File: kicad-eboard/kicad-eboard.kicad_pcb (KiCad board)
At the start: 2 copper layers, 94 parts, among them J1 Conn_02x03, J2 Conn_01x02, J3 Conn_01x10, M1 Hopper_Servo, SW1 LIMIT_1, SW2 LIMIT_2, SW3 SRX_Encoder, U1 TinkerBoard, U10 REF2033, U11 PDQ15-Q24-S12-D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

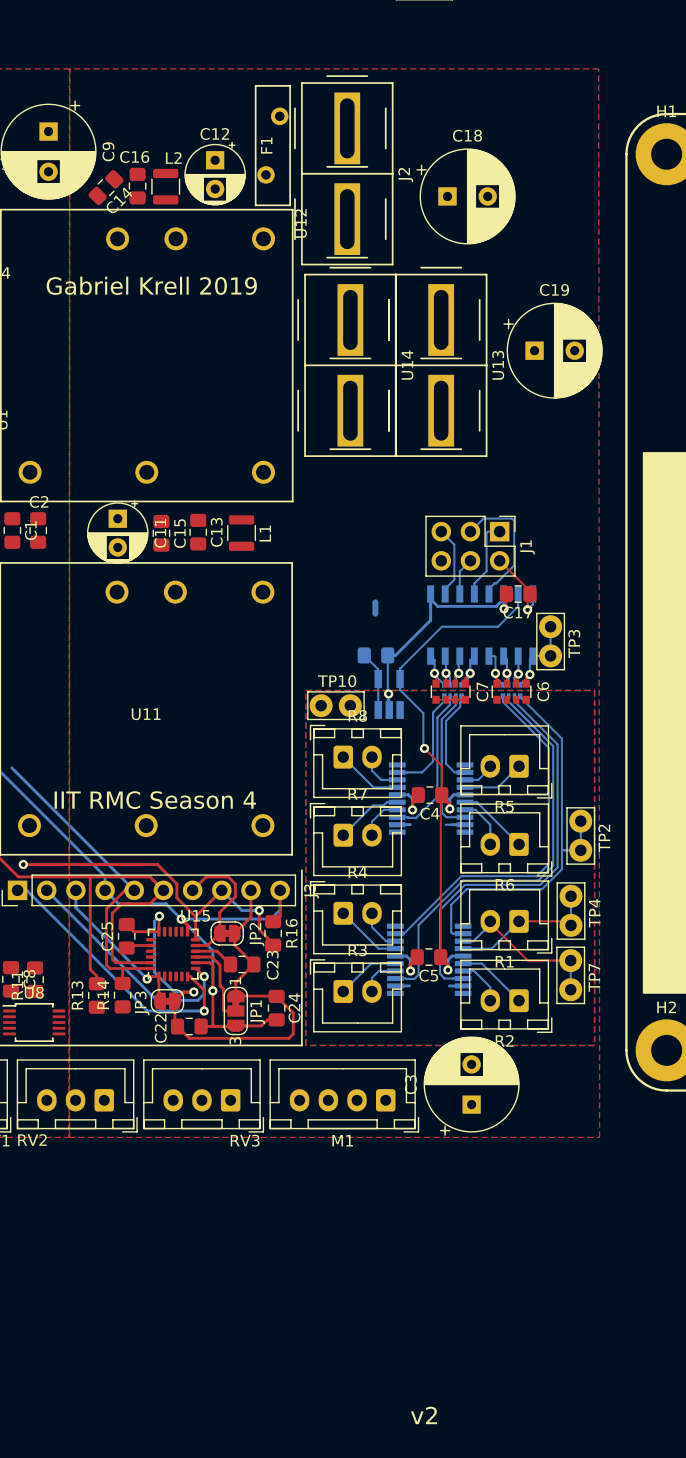
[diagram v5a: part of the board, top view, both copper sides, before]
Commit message: Swap M1,m2 current sense
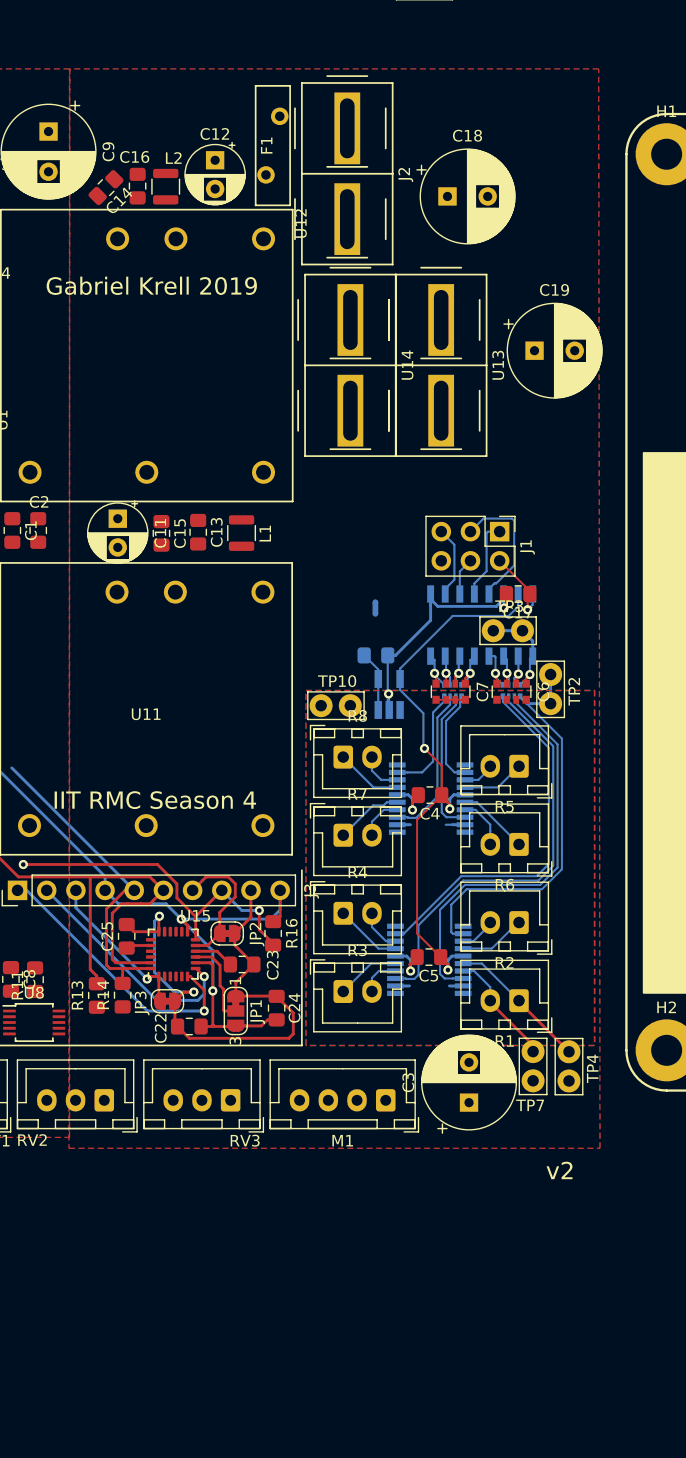
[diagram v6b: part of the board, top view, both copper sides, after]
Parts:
- moved TP4 13.5 mm to (91.3, 100.4)
- moved TP2 13.0 mm to (89.7, 67.5)
- moved TP7 8.58 mm to (88.2, 100.4)
- moved R1 6.90 mm to (87.0, 93.4)
- moved R2 6.80 mm to (87.0, 86.6)
- moved TP3 3.29 mm to (87.2, 61.2), turned to 180 degrees
- moved C3 0.29 mm to (82.6, 102.3)
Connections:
- U6 pad 3: /M1- -> /M2-
- U6 pad 4: /M1+ -> /M2+
- U6 pad 6: /M2+ -> /M1+
- U6 pad 7: /M2- -> /M1-
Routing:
- net /M1-: track 14.3 -> 10.1 mm
- net +3.3VADC: track 47.8 -> 49.5 mm
- net Net-(R9-Pad1): track 35.1 -> 36.4 mm
- net /M1+: track 13.5 -> 12.5 mm
- net Net-(C6-Pad1): track 7.98 -> 9.00 mm
- net /M2-: track 4.12 -> 3.23 mm

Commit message: Routing taking shape
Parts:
- removed C19: 470u, Capacitor_THT:CP_Radial_D8.0mm_P3.50mm
- C10: moved to F.Cu
- moved TP10 16.1 mm to (88.4, 67.6), turned to 90 degrees
- moved C6 14.9 mm to (71.4, 66.2)
- moved R9 14.9 mm to (71.4, 66.1)
- moved J1 9.70 mm to (75.6, 52.3)
- moved TP3 9.70 mm to (77.5, 61.0)
- moved U9 9.70 mm to (74.0, 60.5)
- moved C17 9.70 mm to (77.2, 57.8)
- moved TP2 9.61 mm to (80.2, 66.3)
- moved U10 9.43 mm to (85.1, 66.3)
- moved C10 8.52 mm to (82.6, 65.9), turned to 270 degrees
- moved NT1 7.15 mm to (67.8, 56.7)
- moved C7 4.48 mm to (76.5, 66.3)
- moved R10 4.48 mm to (76.7, 66.2)
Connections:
- TP2 pad 1: Net-(R9-Pad1) -> Net-(R10-Pad1)
- TP3 pad 1: Net-(C6-Pad1) -> Net-(C7-Pad1)
- U9 pad 1: Net-(C6-Pad1) -> Net-(C7-Pad1)
- U9 pad 2: Net-(C6-Pad2) -> Net-(C7-Pad2)
- U9 pad 3: Net-(C6-Pad3) -> Net-(C7-Pad3)
- U9 pad 4: Net-(C6-Pad4) -> Net-(C7-Pad4)
- U9 pad 5: Net-(C7-Pad1) -> Net-(C6-Pad1)
- U9 pad 6: Net-(C7-Pad2) -> Net-(C6-Pad2)
- U9 pad 7: Net-(C7-Pad3) -> Net-(C6-Pad3)
- U9 pad 8: Net-(C7-Pad4) -> Net-(C6-Pad4)
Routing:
- net GNDREF: track 34.2 -> 25.3 mm
- net Net-(R10-Pad1): track 8.40 -> 14.7 mm
- net Net-(R9-Pad1): track 36.4 -> 30.8 mm
- net Net-(C6-Pad1): track 9.00 -> 3.84 mm
- net Net-(C7-Pad1): track 4.04 -> 9.12 mm
- net +5V: track 5.26 -> 9.19 mm, vias 0 -> 1
- net /M1-: track 10.1 -> 12.6 mm
- net /M1+: track 12.5 -> 15.0 mm
- net Net-(R9-Pad4): track 32.1 -> 30.0 mm
- net Net-(R9-Pad3): track 36.7 -> 34.7 mm
- net Net-(R10-Pad4): track 9.59 -> 8.37 mm
- net Net-(R10-Pad2): track 12.9 -> 14.0 mm
- net +3.3VADC: track 49.5 -> 48.7 mm
- net Net-(R9-Pad2): track 36.0 -> 35.2 mm

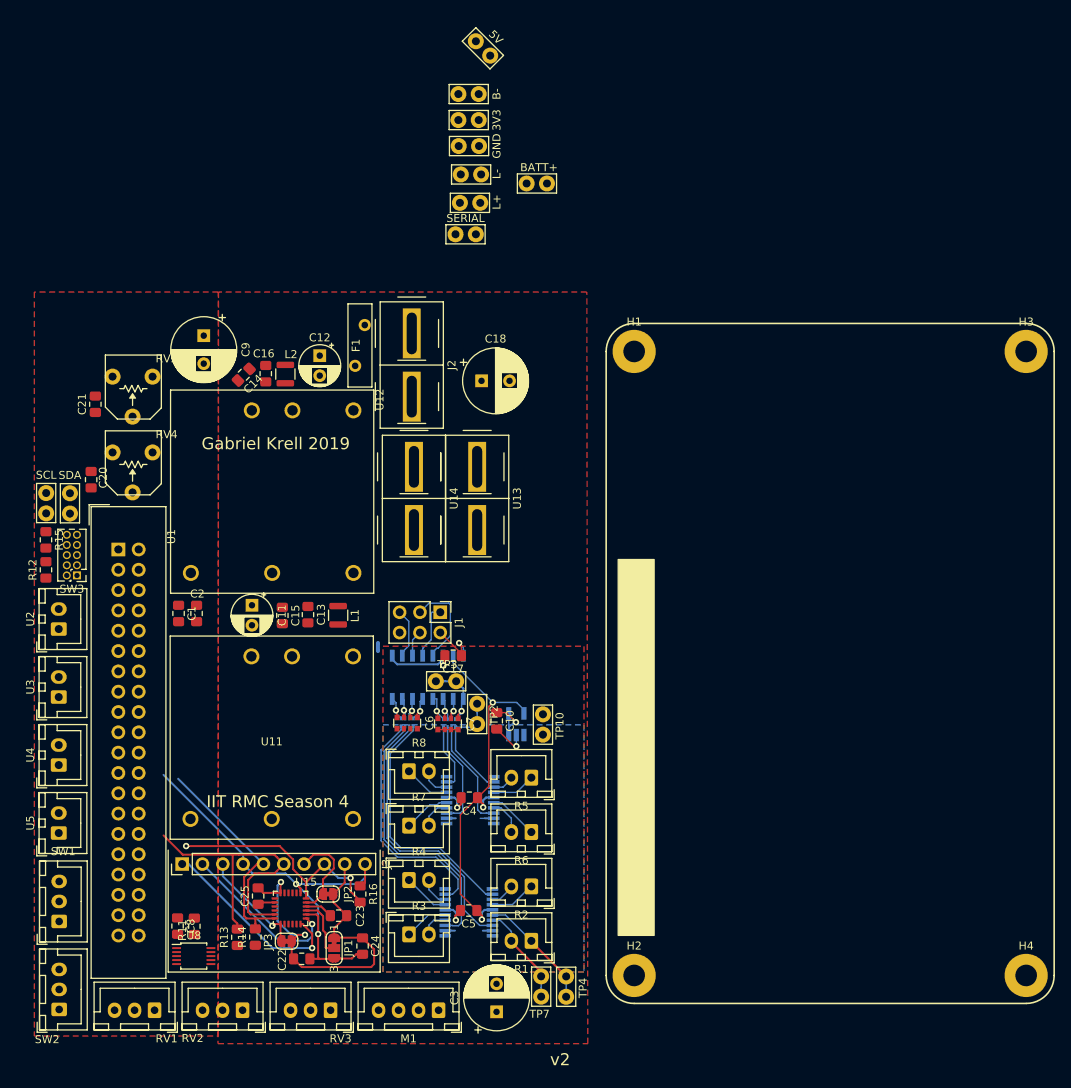
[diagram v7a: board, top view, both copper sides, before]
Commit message: Start moving things in prep for layout
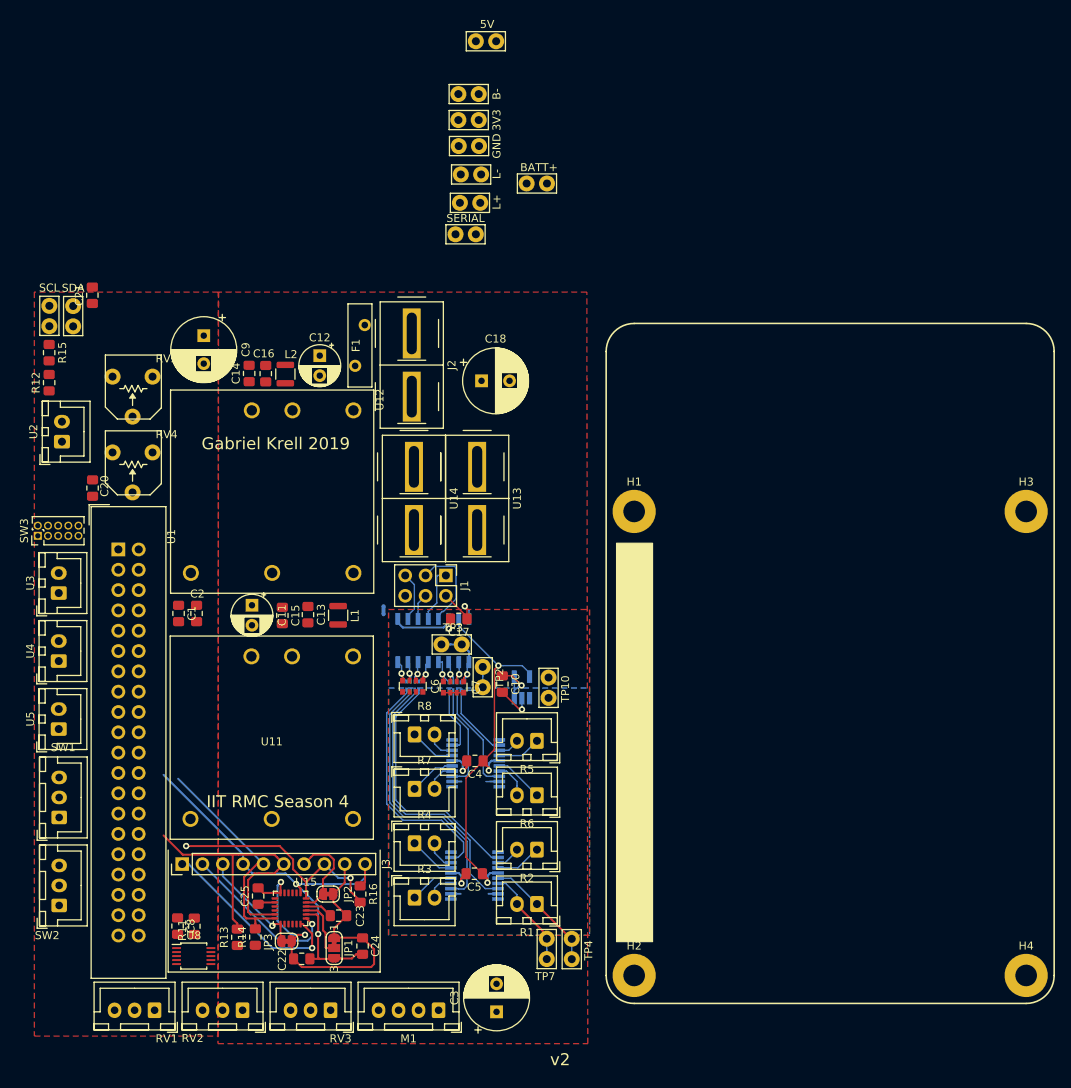
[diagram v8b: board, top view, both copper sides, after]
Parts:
- moved U2 23.4 mm to (28.3, 31.0)
- moved TP5 23.4 mm to (29.7, 14.1)
- moved R12 23.4 mm to (26.7, 23.6)
- moved R15 23.4 mm to (26.7, 19.9)
- moved TP6 23.4 mm to (26.7, 14.0)
- moved H1 20.0 mm to (99.8, 39.7)
- moved H3 20.0 mm to (148.8, 39.7)
- moved C21 13.6 mm to (32.1, 12.7)
- moved SW1 13.0 mm to (27.9, 78.0)
- moved SW2 13.0 mm to (27.9, 89.0)
- moved U3 13.0 mm to (27.9, 49.9)
- moved U4 13.0 mm to (27.9, 58.4)
- moved U5 13.0 mm to (27.9, 66.9)
- moved SW3 6.96 mm to (25.3, 42.8), turned to 90 degrees
- moved TP4 4.75 mm to (92.0, 95.7)
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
